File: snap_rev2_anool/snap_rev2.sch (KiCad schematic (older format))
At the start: 29 parts, among them J1 SJ2-35863B1, P1 CONN_02X05, Q1 TSM2301, SW1 1825910-6, U1 TPS610986, U2 MDBT42Q, Y1 32786Hz

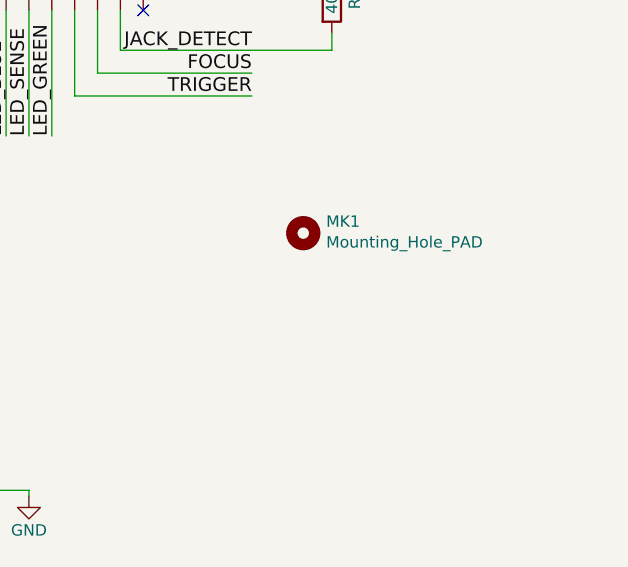
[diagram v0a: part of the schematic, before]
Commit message: camera trigger anool version2
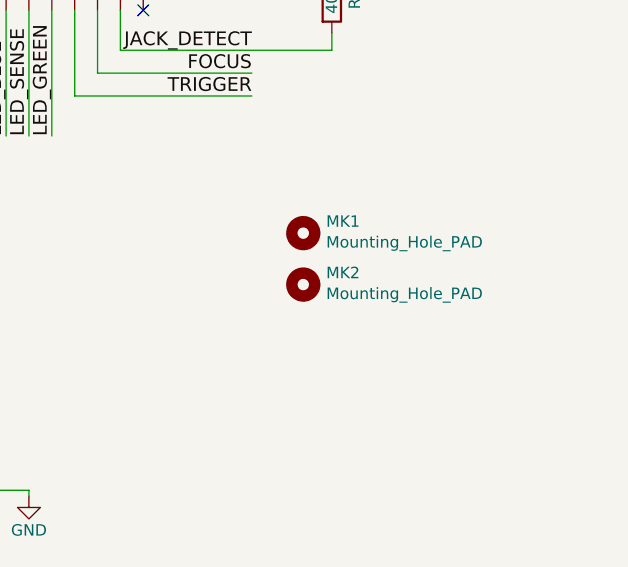
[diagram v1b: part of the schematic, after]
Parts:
- added MK2: Mounting_Hole_PAD, snap_fp:MountingHole_1.7mm_M1.6, symbol Mounting_Hole
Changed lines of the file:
@@
 	4300 875  4300 1025
 Connection ~ 4300 1025
+$Comp
+L Mounting_Hole MK2
+U 1 1 59FB6FBC
+P 7300 5850
+F 0 "MK2" H 7400 5901 50  0000 L CNN
+F 1 "Mounting_Hole_PAD" H 7400 5810 50  0000 L CNN
+F 2 "snap_fp:MountingHole_1.7mm_M1.6" H 7300 5850 50  0001 C CNN
+F 3 "" H 7300 5850 50  0001 C CNN
+	1    7300 5850
+	1    0    0    -1
+$EndComp
 $EndSCHEMATC
